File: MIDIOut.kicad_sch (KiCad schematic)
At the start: 6 parts, among them J401 SJ2-25404B-SMT-TR, U401 74AHC1G125

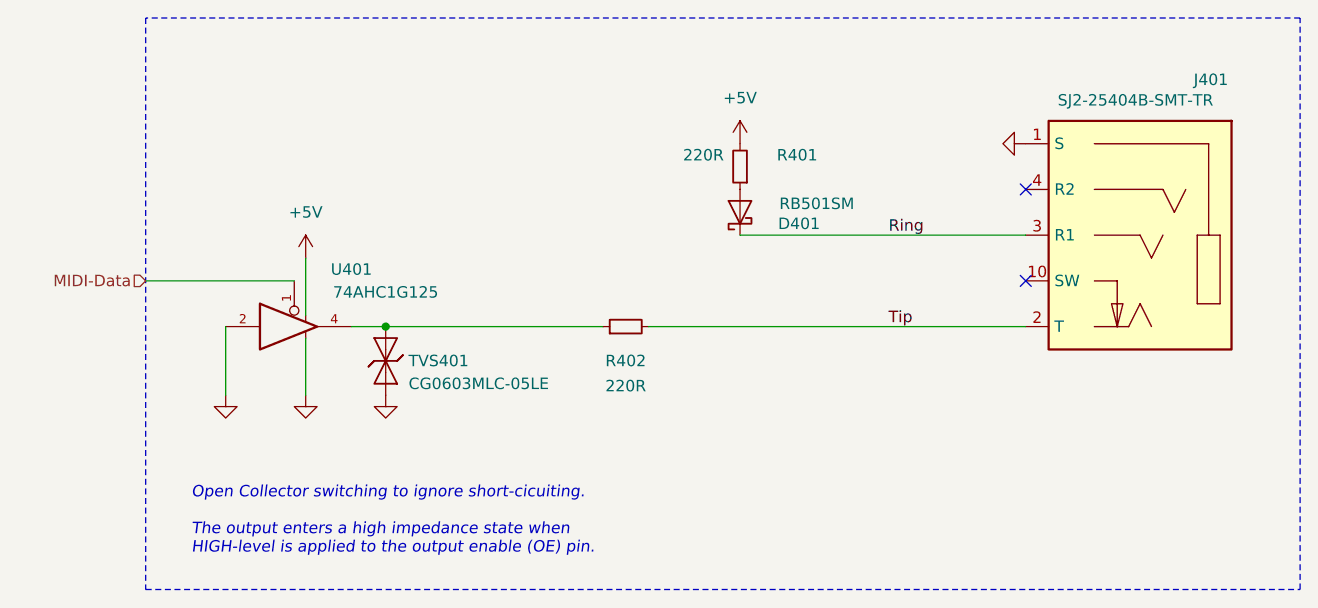
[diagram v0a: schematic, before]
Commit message: Replace diode
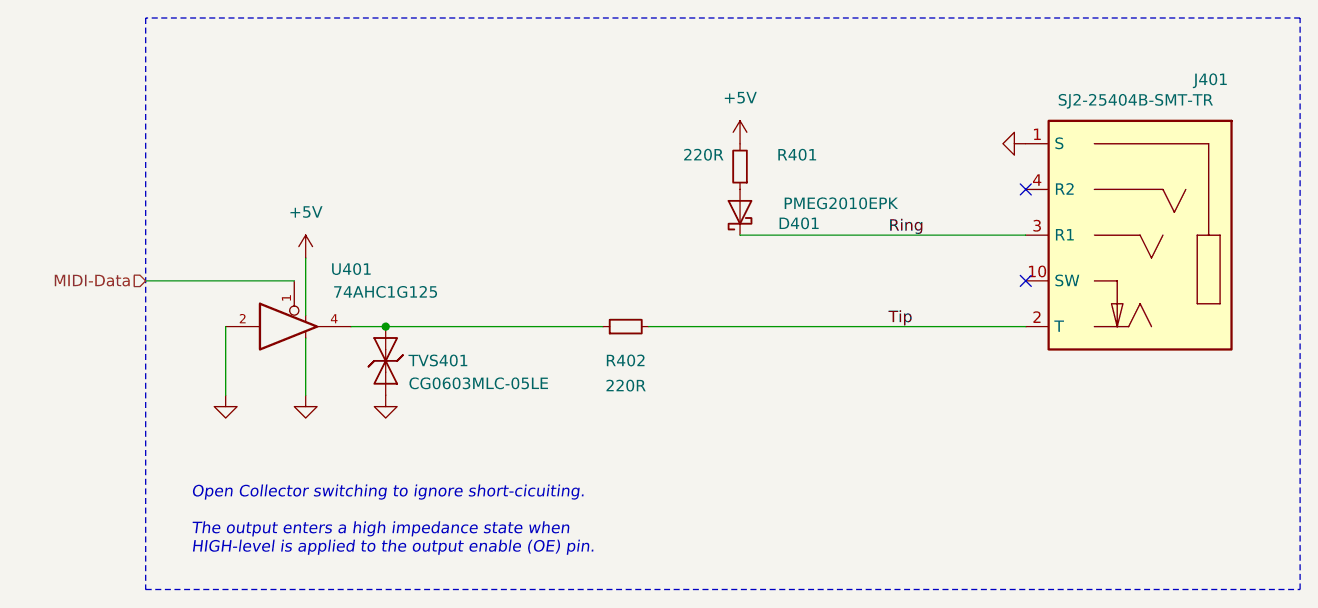
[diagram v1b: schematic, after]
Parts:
- D401: value RB501SM -> PMEG2010EPK; footprint V2_Diode_SMD:D_SOD-523 -> V2_Diode_SMD:D_SOD-1608; symbol V2_Diode:RB501SM -> V2_Diode:PMEG2010EPK; Manufacturer ROHM Semiconductor -> Nexperia; Mouser 755-RB501SM-30FHT2R -> 771-PMEG2010EPK; Product RB501SM-30FHT2R -> PMEG2010EPK; Rating (none) -> 20V
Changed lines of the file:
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@@
 	(title_block
 		(title "MIDI Out")
-		(date "2026-02-12")
-		(rev "2026-02-12")
+		(date "2026-03-12")
+		(rev "2026-03-12")
 	)
 	(text "﻿Open Collector switching to ignore short-cicuiting.\n\nThe output enters a high impedance state when \nHIGH-level is applied to the output enable (OE) pin."
@@
 			)
 		)
-		(property "Description" "Resistor, small symbol"
+		(property "Description" ""
 			(at 154.94 109.22 0)
 			(effects
@@
 			)
 		)
-		(property "Description" "Resistor, small symbol"
+		(property "Description" ""
 			(at 154.94 78.74 0)
 			(effects
@@
 	)
 	(symbol
-		(lib_id "V2_Diode:RB501SM")
+		(lib_id "V2_Diode:PMEG2010EPK")
 		(at 154.94 96.52 90)
 		(unit 1)
@@
 			)
 		)
-		(property "Value" "RB501SM"
-			(at 167.64 95.5676 90)
+		(property "Value" "PMEG2010EPK"
+			(at 172.466 95.5676 90)
 			(effects
 				(font
@@
 			)
 		)
-		(property "Footprint" "V2_Diode_SMD:D_SOD-523"
+		(property "Footprint" "V2_Diode_SMD:D_SOD-1608"
 			(at 161.925 96.52 0)
 			(effects
@@
 			)
 		)
-		(property "Mouser" "755-RB501SM-30FHT2R"
+		(property "Mouser" "771-PMEG2010EPK"
 			(at 170.18 96.52 0)
 			(effects
@@
 			)
 		)
-		(property "Product" "RB501SM-30FHT2R"
+		(property "Product" "PMEG2010EPK"
 			(at 167.64 96.52 0)
 			(effects
@@
 			)
 		)
-		(property "Manufacturer" "ROHM Semiconductor"
+		(property "Manufacturer" "Nexperia "
 			(at 165.1 96.52 0)
 			(effects
 				(font
+					(size 1.27 1.27)
+				)
+				(hide yes)
+			)
+		)
+		(property "Rating" "20V"
+			(at 170.18 96.52 0)
+			(effects
+				(font

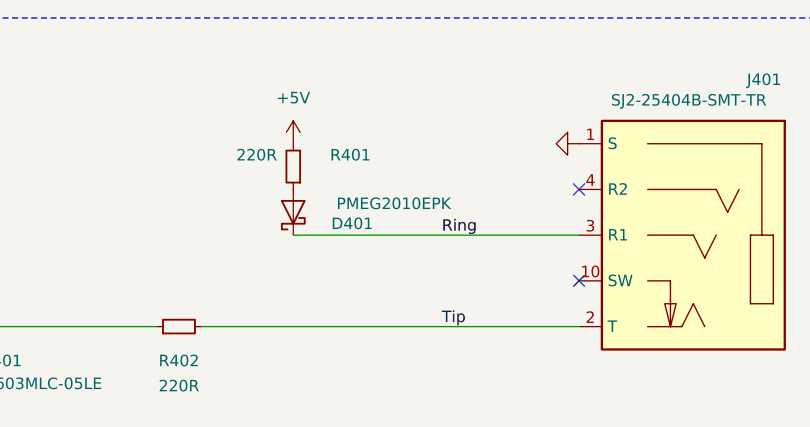
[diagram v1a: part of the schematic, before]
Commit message: Update ESD suppressor
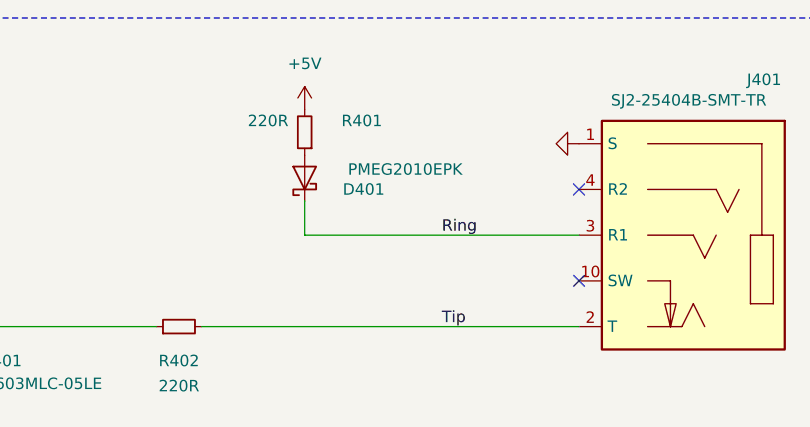
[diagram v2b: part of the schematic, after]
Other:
- moved on the sheet: D401, R401
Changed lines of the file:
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@@
 	(wire
 		(pts
+			(xy 156.21 99.06) (xy 186.69 99.06)
+		)
+		(stroke
+			(width 0)
+			(type default)
+		)
+	)
+	(wire
+		(pts
 			(xy 144.78 109.22) (xy 186.69 109.22)
 		)
@@
 		)
 	)
+	(polyline
+		(pts
+			(xy 217.17 74.93) (xy 88.9 74.93)
+		)
+		(stroke
+			(width 0)
+			(type dash)
+		)
+	)
 	(wire
 		(pts
-			(xy 154.94 99.06) (xy 186.69 99.06)
+			(xy 111.76 109.22) (xy 115.57 109.22)
 		)
 		(stroke
@@
 		)
 	)
+	(wire
+		(pts
+			(xy 115.57 109.22) (xy 139.7 109.22)
+		)
+		(stroke
+			(width 0)
+			(type default)
+		)
+	)
+	(wire
+		(pts
+			(xy 97.79 109.22) (xy 97.79 116.84)
+		)
+		(stroke
+			(width 0)
+			(type default)
+		)
+	)
+	(wire
+		(pts
+			(xy 106.68 110.49) (xy 106.68 116.84)
+		)
+		(stroke
+			(width 0)
+			(type default)
+		)
+	)
+	(wire
+		(pts
+			(xy 106.68 101.6) (xy 106.68 107.95)
+		)
+		(stroke
+			(width 0)
+			(type default)
+		)
+	)
 	(polyline
 		(pts
-			(xy 217.17 74.93) (xy 88.9 74.93)
+			(xy 217.17 138.43) (xy 217.17 74.93)
 		)
 		(stroke
@@
 		)
 	)
+	(polyline
+		(pts
+			(xy 88.9 138.43) (xy 217.17 138.43)
+		)
+		(stroke
+			(width 0)
+			(type dash)
+		)
+	)
+	(polyline
+		(pts
+			(xy 88.9 74.93) (xy 88.9 138.43)
+		)
+		(stroke
+			(width 0)
+			(type dash)
+		)
+	)
 	(wire
 		(pts
-			(xy 111.76 109.22) (xy 115.57 109.22)
+			(xy 156.21 95.25) (xy 156.21 99.06)
 		)
 		(stroke
 			(width 0)
 			(type default)
-		)
-	)
-	(wire
-		(pts
-			(xy 115.57 109.22) (xy 139.7 109.22)
-		)
-		(stroke
-			(width 0)
-			(type default)
-		)
-	)
-	(wire
-		(pts
-			(xy 97.79 109.22) (xy 97.79 116.84)
-		)
-		(stroke
-			(width 0)
-			(type default)
-		)
-	)
-	(wire
-		(pts
-			(xy 106.68 110.49) (xy 106.68 116.84)
-		)
-		(stroke
-			(width 0)
-			(type default)
-		)
-	)
-	(wire
-		(pts
-			(xy 106.68 101.6) (xy 106.68 107.95)
-		)
-		(stroke
-			(width 0)
-			(type default)
-		)
-	)
-	(polyline
-		(pts
-			(xy 217.17 138.43) (xy 217.17 74.93)
-		)
-		(stroke
-			(width 0)
-			(type dash)
-		)
-	)
-	(polyline
-		(pts
-			(xy 88.9 138.43) (xy 217.17 138.43)
-		)
-		(stroke
-			(width 0)
-			(type dash)
-		)
-	)
-	(polyline
-		(pts
-			(xy 88.9 74.93) (xy 88.9 138.43)
-		)
-		(stroke
-			(width 0)
-			(type dash)
 		)
 	)
@@
 	(symbol
 		(lib_id "V2_Resistor:0603_220R")
-		(at 154.94 91.44 180)
+		(at 156.21 87.63 180)
 		(unit 1)
 		(exclude_from_sim no)
@@
 		(dnp no)
 		(property "Reference" "R401"
-			(at 161.29 90.17 0)
+			(at 162.56 86.36 0)
 			(effects
 				(font
@@
 		)
 		(property "Value" "220R"
-			(at 150.876 90.17 0)
+			(at 152.146 86.36 0)
 			(effects
 				(font
@@
 		)
 		(property "Footprint" "V2_Resistor_SMD:R_0603"
-			(at 154.94 75.692 0)
+			(at 156.21 71.882 0)
 			(effects
 				(font
@@
 		)
 		(property "Datasheet" ""
-			(at 154.94 91.44 0)
+			(at 156.21 87.63 0)
 			(effects
 				(font
@@
 		)
 		(property "Description" ""
-			(at 154.94 78.74 0)
+			(at 156.21 74.93 0)
 			(effects
 				(font
@@
 		)
 		(property "Mouser" "71-CRCW0603220RFKEAH"
-			(at 154.94 68.58 0)
+			(at 156.21 64.77 0)
 			(effects
 				(font
@@
 		)
 		(property "Product" "CRCW0603220RFKEAHP"
-			(at 154.94 73.66 0)
+			(at 156.21 69.85 0)
 			(effects
 				(font
@@
 		)
 		(property "Manufacturer" "Vishay"
-			(at 154.94 76.2 0)
+			(at 156.21 72.39 0)
 			(effects
 				(font
@@
 		)
 		(property "Rating" "330mW"
-			(at 154.94 71.12 0)
+			(at 156.21 67.31 0)
 			(effects
 				(font
@@
 	(symbol
 		(lib_id "V2_Diode:PMEG2010EPK")
-		(at 154.94 96.52 90)
+		(at 156.21 92.71 90)
 		(unit 1)
 		(exclude_from_sim no)
@@
 		(dnp no)
 		(property "Reference" "D401"
-			(at 163.83 97.79 90)
+			(at 165.1 93.98 90)
 			(effects
 				(font
@@
 		)
 		(property "Value" "PMEG2010EPK"
-			(at 172.466 95.5676 90)
+			(at 173.736 91.7576 90)
 			(effects
 				(font
@@
 		)
 		(property "Footprint" "V2_Diode_SMD:D_SOD-1608"
-			(at 161.925 96.52 0)
+			(at 163.195 92.71 0)
 			(effects
 				(font
@@
 		)
 		(property "Datasheet" ""
-			(at 154.94 96.52 0)
+			(at 156.21 92.71 0)
 			(effects
 				(font
@@
 		)
 		(property "Description" ""
-			(at 154.94 96.52 0)
+			(at 156.21 92.71 0)
 			(effects
 				(font
@@
 		)
 		(property "Mouser" "771-PMEG2010EPK"
-			(at 170.18 96.52 0)
+			(at 171.45 92.71 0)
 			(effects
 				(font
@@
 		)
 		(property "Product" "PMEG2010EPK"
-			(at 167.64 96.52 0)
+			(at 168.91 92.71 0)
 			(effects
 				(font
@@
 		)
 		(property "Manufacturer" "Nexperia "
-			(at 165.1 96.52 0)
+			(at 166.37 92.71 0)
 			(effects
 				(font
@@
 		)
 		(property "Rating" "20V"
-			(at 170.18 96.52 0)
+			(at 171.45 92.71 0)
 			(effects
 				(font
@@
 	(symbol
 		(lib_id "V2_power:+5V")
-		(at 154.94 88.9 0)
+		(at 156.21 85.09 0)
 		(unit 1)
 		(exclude_from_sim no)
@@
 		(fields_autoplaced yes)
 		(property "Reference" "#PWR401"
-			(at 154.94 92.71 0)
+			(at 156.21 88.9 0)
 			(effects
 				(font
@@
 		)
 		(property "Value" "+5V"
-			(at 154.94 83.82 0)
+			(at 156.21 80.01 0)
 			(effects
 				(font
@@
 		)
 		(property "Footprint" ""
-			(at 154.94 88.9 0)
+			(at 156.21 85.09 0)
 			(effects
 				(font
@@
 		)
 		(property "Datasheet" ""
-			(at 154.94 88.9 0)
+			(at 156.21 85.09 0)
 			(effects
 				(font
@@
 		)
 		(property "Description" ""
-			(at 154.94 88.9 0)
-			(effects
-				(font
+			(at 156.21 85.09 0)
+			(effects
+				(font

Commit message: KiCad 10
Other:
- company: (none) -> Versio Duo

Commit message: Refresh
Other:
- title: MIDI Out -> V2 connect
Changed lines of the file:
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@@
 	(paper "A4")
 	(title_block
-		(title "MIDI Out")
-		(date "2026-03-24")
+		(title "V2 connect")
+		(date "2026-03-26")
 		(rev "2026-03-14")
 		(company "Versio Duo")
